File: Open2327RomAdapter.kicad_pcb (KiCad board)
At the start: 2 copper layers, 19.6 x 43.2 mm, 7 parts, among them P1 CONN_01X04, U1 2364, U2 27128

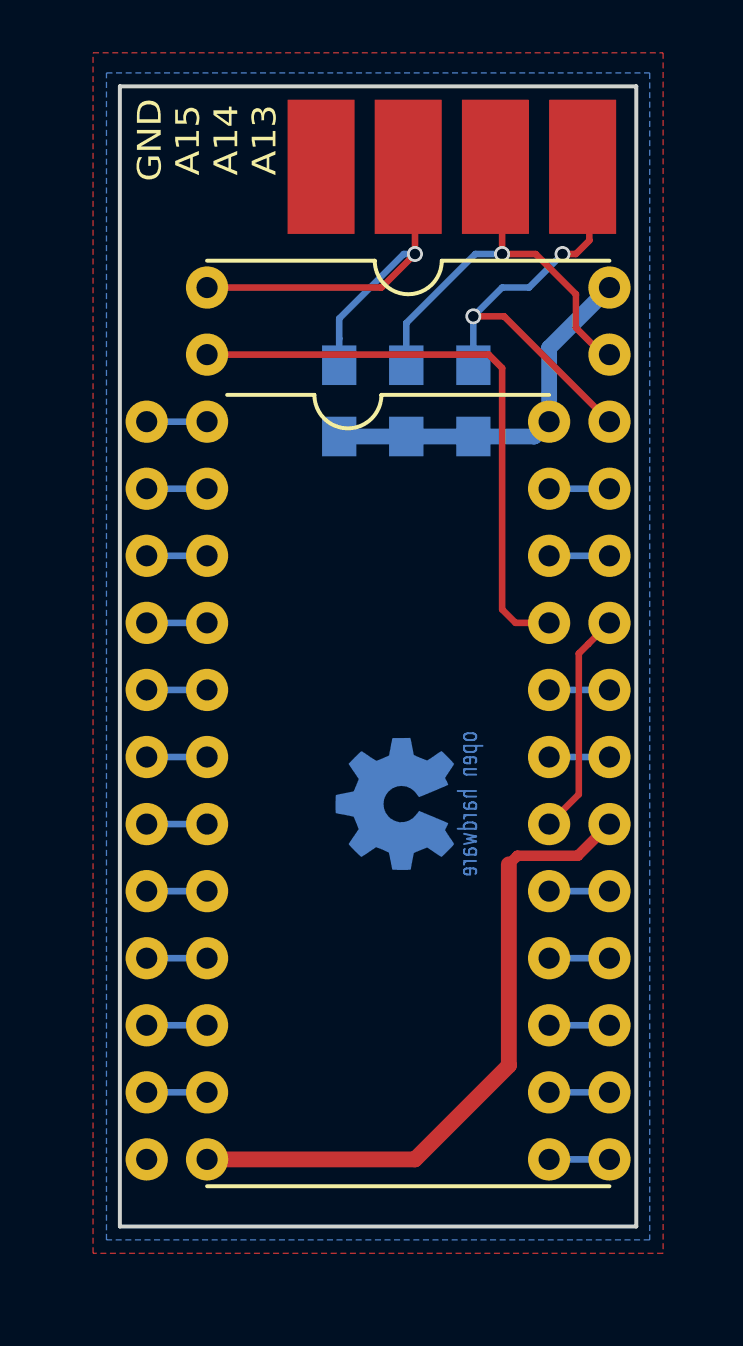
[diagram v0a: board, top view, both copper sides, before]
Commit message: Fix URL, better ground plane, round corners
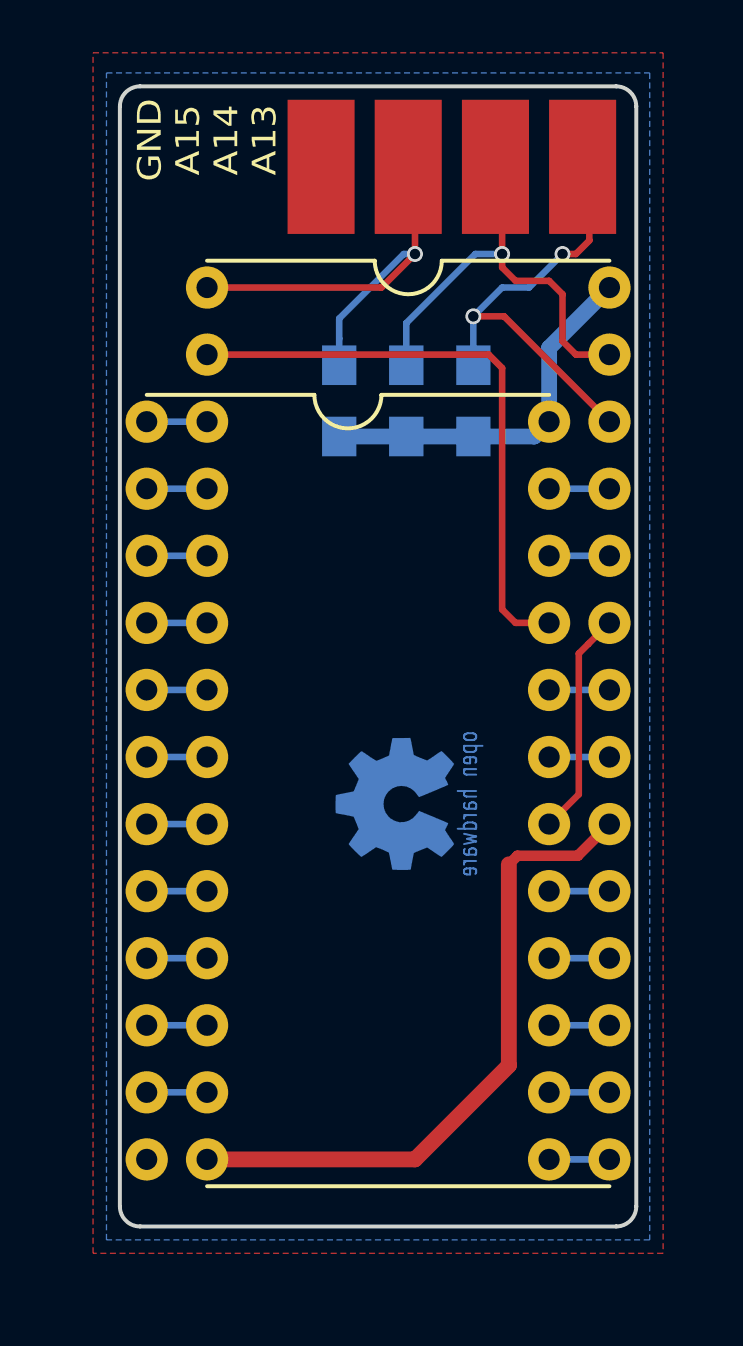
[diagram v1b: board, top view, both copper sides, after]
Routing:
- net Net-(P1-Pad3): track 16.0 -> 16.6 mm
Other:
- outline, holes or cut-outs redrawn
- rule pad_to_mask_clearance: 0.2 -> 0
- board text added: "github.com/SukkoPera/Open2327RomAdapter"
- board text removed: "https://github.com/SukkoPera/Open2327RomAdapter"

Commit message: Final touches for V2
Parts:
- moved G*** 1.48 mm to (154.4, 121.9)
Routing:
- net GND: track 25.0 -> 66.8 mm, vias 0 -> 12
- net Net-(U1-Pad18): track 8.57 -> 12.2 mm
- net Net-(P1-Pad2): track 17.4 -> 16.7 mm
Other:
- board text added: "V2"
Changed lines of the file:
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@@
     (area 145.212999 93.904999 164.921001 137.235001)
     (thickness 1.6)
-    (drawings 13)
-    (tracks 72)
+    (drawings 14)
+    (tracks 95)
     (zones 0)
     (modules 7)
@@
   )
   (page A4)
+  (title_block
+    (title "Open2327RomAdapter: C64 ROM 24 -> EPROM 28 Pin Adapter")
+    (date 2018-01-05)
+    (rev 2)
+    (company SukkoPera)
+    (comment 1 https://ist.uwaterloo.ca/~~schepers/sockets.html)
+    (comment 2 https://ist.uwaterloo.ca/~~schepers/roms.html)
+  )
   (layers
     (0 F.Cu signal)
@@
   )
   (module w_logo:Logo_copper_OSHW_6x6mm (layer B.Cu)
-    (at 155.702 121.158 270)
+    (at 154.432 121.92 270)
     (descr "Open Hardware Logo, 6x6mm")
     (fp_text reference G*** (at 0 0 270) (layer B.SilkS) hide
@@
     )
   )
+  (gr_text V2 (at 163.83 95.504 90) (layer B.SilkS)
+    (effects (font (size 1 1) (thickness 0.15)) (justify mirror))
+  )
   (gr_arc (start 164.084 136.398) (end 164.846 136.398) (angle 90) (layer Edge.Cuts) (width 0.15))
   (gr_arc (start 146.05 136.398) (end 146.05 137.16) (angle 90) (layer Edge.Cuts) (width 0.15))
@@
     (arrow2b (pts (xy 170.18 93.98) (xy 170.766421 95.106504)))
   )
-  (gr_text github.com/SukkoPera/Open2327RomAdapter (at 151.13 115.316 90) (layer B.SilkS)
+  (gr_text github.com/SukkoPera/Open2327RomAdapter (at 150.622 115.316 90) (layer B.SilkS)
     (effects (font (size 1 1) (thickness 0.15)) (justify mirror))
   )
@@
   (gr_line (start 164.846 136.398) (end 164.846 94.742) (layer Edge.Cuts) (width 0.15))
   (gr_line (start 146.05 137.16) (end 164.084 137.16) (layer Edge.Cuts) (width 0.15))
-  (segment (start 160.02 131.064) (end 160.02 123.444) (width 0.6) (layer F.Cu) (net 1))
-  (segment (start 160.343999 123.120001) (end 160.02 123.444) (width 0.4) (layer F.Cu) (net 1))
-  (segment (start 163.83 121.92) (end 162.629999 123.120001) (width 0.4) (layer F.Cu) (net 1))
-  (segment (start 162.629999 123.120001) (end 160.343999 123.120001) (width 0.4) (layer F.Cu) (net 1))
-  (segment (start 156.464 134.62) (end 160.02 131.064) (width 0.6) (layer F.Cu) (net 1))
-  (segment (start 148.59 134.62) (end 156.464 134.62) (width 0.6) (layer F.Cu) (net 1))
+  (segment (start 158.242 134.62) (end 151.892 134.62) (width 0.6) (layer B.Cu) (net 1))
+  (via (at 151.892 134.62) (size 0.8) (drill 0.6) (layers F.Cu B.Cu) (net 1))
+  (segment (start 158.242 129.54) (end 158.242 134.62) (width 0.6) (layer F.Cu) (net 1))
+  (via (at 158.242 134.62) (size 0.8) (drill 0.6) (layers F.Cu B.Cu) (net 1))
+  (segment (start 158.242 124.46) (end 158.242 129.54) (width 0.6) (layer B.Cu) (net 1))
+  (via (at 158.242 129.54) (size 0.8) (drill 0.6) (layers F.Cu B.Cu) (net 1))
+  (segment (start 158.242 119.38) (end 158.242 124.46) (width 0.6) (layer F.Cu) (net 1))
+  (via (at 158.242 124.46) (size 0.8) (drill 0.6) (layers F.Cu B.Cu) (net 1))
+  (segment (start 158.242 114.3) (end 158.242 119.38) (width 0.6) (layer B.Cu) (net 1))
+  (via (at 158.242 119.38) (size 0.8) (drill 0.6) (layers F.Cu B.Cu) (net 1))
+  (segment (start 158.242 109.22) (end 158.242 114.3) (width 0.6) (layer F.Cu) (net 1))
+  (via (at 158.242 114.3) (size 0.8) (drill 0.6) (layers F.Cu B.Cu) (net 1))
+  (segment (start 151.892 109.22) (end 158.242 109.22) (width 0.6) (layer B.Cu) (net 1))
+  (via (at 158.242 109.22) (size 0.8) (drill 0.6) (layers F.Cu B.Cu) (net 1))
+  (segment (start 151.892 114.3) (end 151.892 109.22) (width 0.6) (layer F.Cu) (net 1))
+  (via (at 151.892 109.22) (size 0.8) (drill 0.6) (layers F.Cu B.Cu) (net 1))
+  (segment (start 151.892 119.38) (end 151.892 114.3) (width 0.6) (layer B.Cu) (net 1))
+  (via (at 151.892 114.3) (size 0.8) (drill 0.6) (layers F.Cu B.Cu) (net 1))
+  (segment (start 151.892 124.46) (end 151.892 119.38) (width 0.6) (layer F.Cu) (net 1))
+  (via (at 151.892 119.38) (size 0.8) (drill 0.6) (layers F.Cu B.Cu) (net 1))
+  (segment (start 151.892 129.54) (end 151.892 124.46) (width 0.6) (layer B.Cu) (net 1))
+  (via (at 151.892 124.46) (size 0.8) (drill 0.6) (layers F.Cu B.Cu) (net 1))
+  (segment (start 148.59 134.62) (end 151.892 134.62) (width 0.6) (layer F.Cu) (net 1))
+  (segment (start 151.892 134.62) (end 151.892 129.54) (width 0.6) (layer F.Cu) (net 1))
+  (via (at 151.892 129.54) (size 0.8) (drill 0.6) (layers F.Cu B.Cu) (net 1))
   (segment (start 158.675098 107.241724) (end 160.982276 107.241724) (width 0.6) (layer B.Cu) (net 2))
   (segment (start 160.982276 107.241724) (end 161.544 106.68) (width 0.6) (layer B.Cu) (net 2))
@@
   (segment (start 161.544 127) (end 163.83 127) (width 0.25) (layer B.Cu) (net 17))
   (segment (start 161.544 124.46) (end 163.83 124.46) (width 0.25) (layer B.Cu) (net 18))
-  (segment (start 161.544 121.92) (end 162.669001 120.794999) (width 0.25) (layer F.Cu) (net 19))
-  (segment (start 162.669001 115.460999) (end 163.030001 115.099999) (width 0.25) (layer F.Cu) (net 19))
-  (segment (start 162.669001 120.794999) (end 162.669001 115.460999) (width 0.25) (layer F.Cu) (net 19))
-  (segment (start 163.030001 115.099999) (end 163.83 114.3) (width 0.25) (layer F.Cu) (net 19))
+  (segment (start 161.544 121.92) (end 160.274 121.92) (width 0.25) (layer F.Cu) (net 19))
+  (segment (start 159.766 121.412) (end 159.766 115.968999) (width 0.25) (layer F.Cu) (net 19))
+  (segment (start 160.274 121.92) (end 159.766 121.412) (width 0.25) (layer F.Cu) (net 19))
+  (segment (start 159.766 115.968999) (end 160.274 115.460999) (width 0.25) (layer F.Cu) (net 19))
+  (segment (start 160.274 115.460999) (end 162.669001 115.460999) (width 0.25) (layer F.Cu) (net 19))
+  (segment (start 162.669001 115.460999) (end 163.83 114.3) (width 0.25) (layer F.Cu) (net 19))
   (segment (start 161.544 119.38) (end 163.83 119.38) (width 0.25) (layer B.Cu) (net 20))
   (segment (start 161.544 116.84) (end 163.83 116.84) (width 0.25) (layer B.Cu) (net 21))
@@
   (segment (start 161.544 111.76) (end 163.83 111.76) (width 0.25) (layer B.Cu) (net 23))
   (segment (start 161.544 109.22) (end 163.83 109.22) (width 0.25) (layer B.Cu) (net 24))
-  (segment (start 148.59 101.6) (end 155.194 101.6) (width 0.25) (layer F.Cu) (net 25))
-  (segment (start 155.194 101.6) (end 156.464 100.33) (width 0.25) (layer F.Cu) (net 25))
-  (segment (start 156.464 100.33) (end 156.039736 100.33) (width 0.25) (layer B.Cu) (net 25))
-  (segment (start 156.039736 100.33) (end 153.595098 102.774638) (width 0.25) (layer B.Cu) (net 25))
-  (segment (start 153.595098 102.774638) (end 153.595098 103.541724) (width 0.25) (layer B.Cu) (net 25))
-  (segment (start 153.595098 103.541724) (end 153.595098 104.541724) (width 0.25) (layer B.Cu) (net 25))
-  (via (at 156.464 100.33) (size 0.6) (drill 0.4) (layers F.Cu B.Cu) (net 25))
-  (segment (start 156.464 97.028) (end 156.464 100.33) (width 0.25) (layer F.Cu) (net 25))
-  (segment (start 159.766 100.33) (end 159.766 100.838) (width 0.25) (layer F.Cu) (net 26))
-  (segment (start 159.766 100.838) (end 160.274 101.346) (width 0.25) (layer F.Cu) (net 26))
-  (segment (start 160.274 101.346) (end 161.544 101.346) (width 0.25) (layer F.Cu) (net 26))
+  (segment (start 153.595098 104.541724) (end 153.595098 102.944902) (width 0.25) (layer B.Cu) (net 25))
+  (segment (start 153.595098 102.944902) (end 153.924 102.616) (width 0.25) (layer B.Cu) (net 25))
+  (segment (start 153.924 102.616) (end 156.21 100.33) (width 0.25) (layer B.Cu) (net 25))
+  (via (at 156.21 100.33) (size 0.6) (drill 0.4) (layers F.Cu B.Cu) (net 25))
+  (segment (start 148.59 101.6) (end 154.94 101.6) (width 0.25) (layer F.Cu) (net 25))
+  (segment (start 156.21 100.33) (end 154.94 101.6) (width 0.25) (layer F.Cu) (net 25))
+  (segment (start 156.21 97.028) (end 156.21 100.33) (width 0.25) (layer F.Cu) (net 25))
+  (segment (start 160.528 101.346) (end 161.544 101.346) (width 0.25) (layer F.Cu) (net 26))
+  (segment (start 159.512 100.33) (end 159.512 100.754264) (width 0.25) (layer F.Cu) (net 26))
+  (segment (start 159.512 100.754264) (end 160.103736 101.346) (width 0.25) (layer F.Cu) (net 26))
+  (segment (start 160.103736 101.346) (end 160.528 101.346) (width 0.25) (layer F.Cu) (net 26))
+  (segment (start 159.512 100.33) (end 158.75 100.33) (width 0.25) (layer B.Cu) (net 26))
+  (segment (start 159.512 97.028) (end 159.512 100.33) (width 0.25) (layer F.Cu) (net 26))
+  (via (at 159.512 100.33) (size 0.6) (drill 0.4) (layers F.Cu B.Cu) (net 26))
   (segment (start 162.56 104.14) (end 163.83 104.14) (width 0.25) (layer F.Cu) (net 26))
   (segment (start 161.544 101.346) (end 162.052 101.854) (width 0.25) (layer F.Cu) (net 26))
   (segment (start 162.052 101.854) (end 162.052 103.632) (width 0.25) (layer F.Cu) (net 26))
   (segment (start 162.052 103.632) (end 162.56 104.14) (width 0.25) (layer F.Cu) (net 26))
-  (segment (start 159.766 97.028) (end 159.766 100.33) (width 0.25) (layer F.Cu) (net 26))
-  (via (at 159.766 100.33) (size 0.6) (drill 0.4) (layers F.Cu B.Cu) (net 26))
   (segment (start 158.75 100.33) (end 156.135098 102.944902) (width 0.25) (layer B.Cu) (net 26))
-  (segment (start 159.766 100.33) (end 158.75 100.33) (width 0.25) (layer B.Cu) (net 26))
   (segment (start 156.135098 102.944902) (end 156.135098 104.541724) (width 0.25) (layer B.Cu) (net 26))
+  (segment (start 162.814 99.818) (end 162.81 99.822) (width 0.25) (layer F.Cu) (net 27))
+  (segment (start 162.81 100.076) (end 162.556 100.33) (width 0.25) (layer F.Cu) (net 27))
+  (segment (start 162.814 97.028) (end 162.814 99.818) (width 0.25) (layer F.Cu) (net 27))
+  (segment (start 162.81 99.822) (end 162.81 100.076) (width 0.25) (layer F.Cu) (net 27))
   (segment (start 162.556 100.33) (end 162.052 100.33) (width 0.25) (layer F.Cu) (net 27))
-  (segment (start 163.068 97.028) (end 163.068 99.818) (width 0.25) (layer F.Cu) (net 27))
-  (segment (start 163.068 99.818) (end 162.556 100.33) (width 0.25) (layer F.Cu) (net 27))
   (via (at 162.052 100.33) (size 0.6) (drill 0.4) (layers F.Cu B.Cu) (net 27))
   (segment (start 162.052 100.33) (end 160.782 101.6) (width 0.25) (layer B.Cu) (net 27))

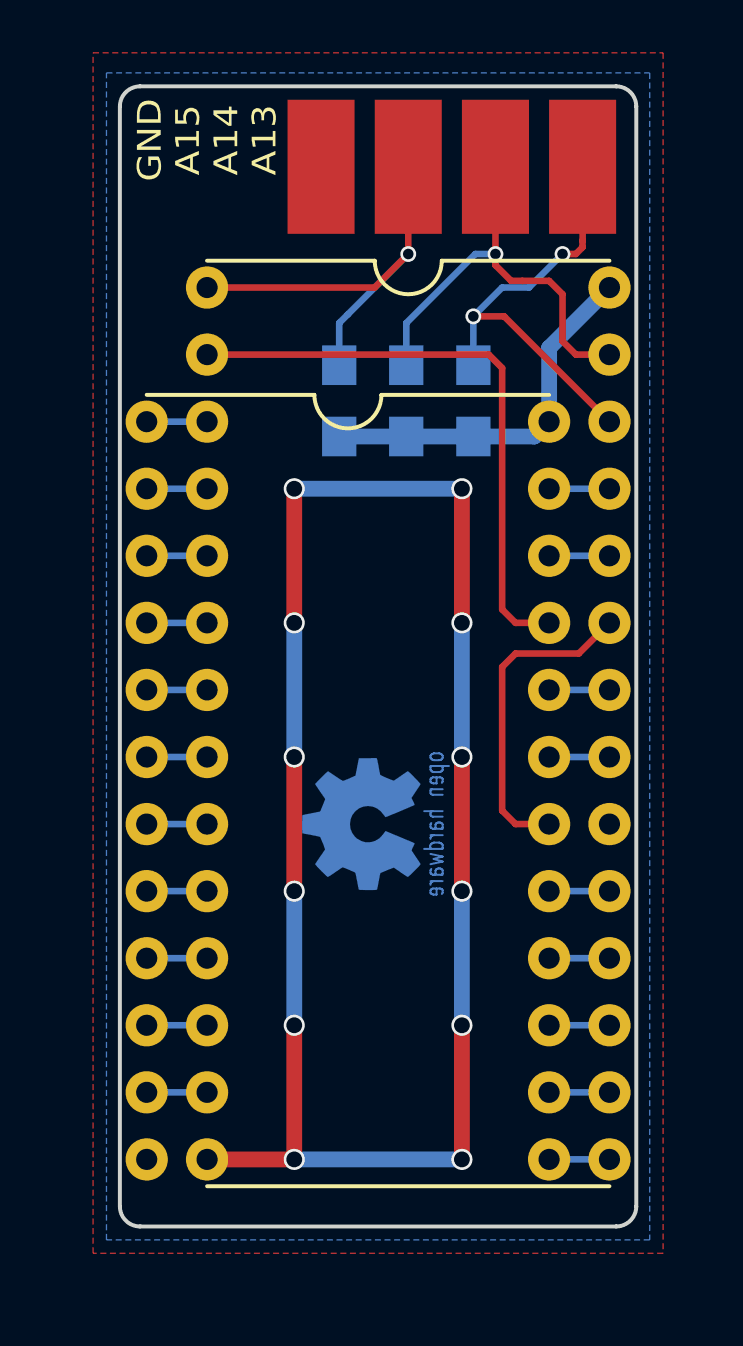
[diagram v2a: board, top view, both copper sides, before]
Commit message: Move solderable pads to 0.1" pitch and drill a hole through them Also port to Kicad 5 and use builtin components/footprints
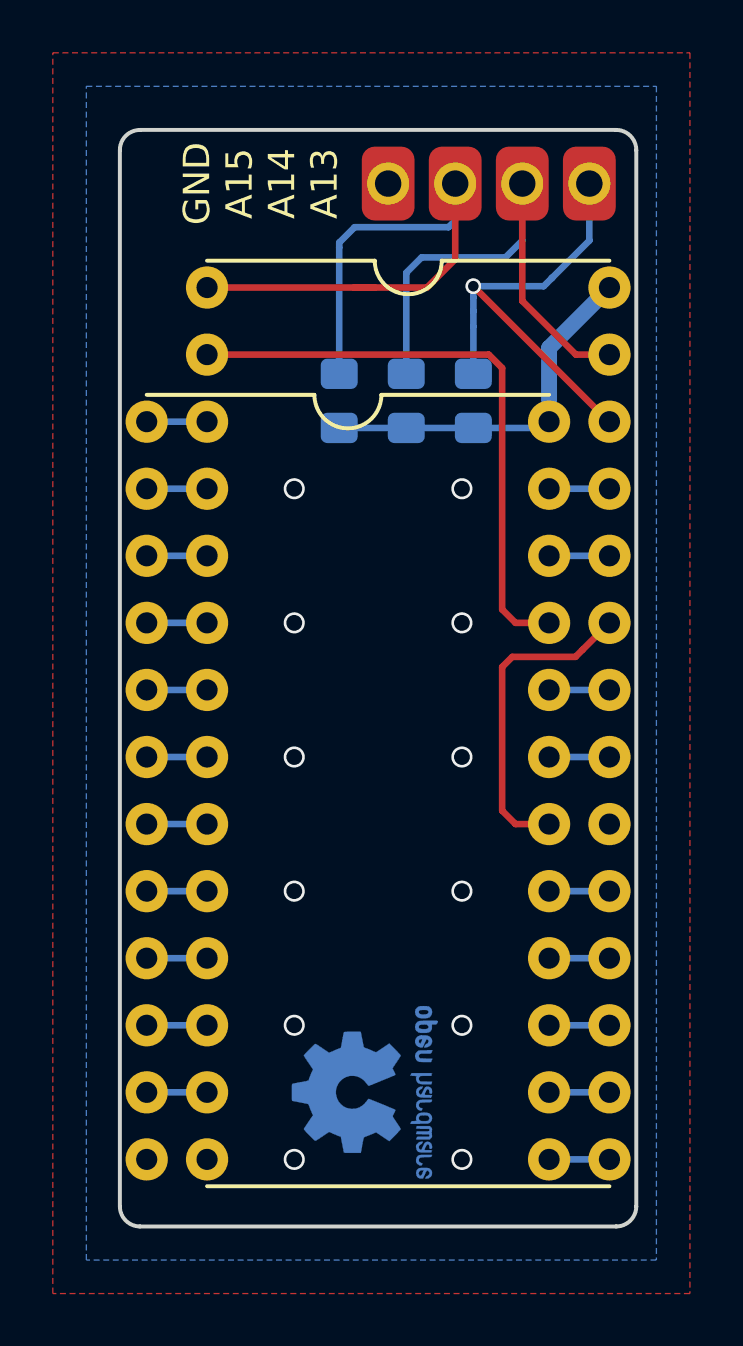
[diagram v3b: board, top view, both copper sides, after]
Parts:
- removed G***: LOGO, w_logo:Logo_copper_OSHW_6x6mm
- added P99: OSHW_LOGO, Symbol:OSHW-Logo2_7.3x6mm_Copper, B.Cu at (154.6, 132.1)
- P1: value CONN_01X04 -> Conn_01x04; footprint Open2327RomAdapter:LoosePads-4 -> Open2327RomAdapter:Solderable_PinHeader_1x04
- R1, R2, R3: value 10K -> 10k; footprint Resistors_SMD:R_0805_HandSoldering -> Resistor_SMD:R_0805_2012Metric_Pad1.15x1.40mm_HandSolder
- moved P1 2.62 mm to (155.4, 97.7), turned to 90 degrees
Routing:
- net GND: track 66.8 -> 0.00 mm
- net Net-(P1-Pad2): track 16.7 -> 24.6 mm, vias 1 -> 0
- net Net-(P1-Pad3): track 16.5 -> 19.5 mm, vias 1 -> 0
- net Net-(P1-Pad4): track 16.9 -> 17.9 mm, vias 2 -> 1
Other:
- board size 19.6 x 43.2 mm -> 19.6 x 41.5 mm
- board text added: "Licensed under CERN OHL v.1.2"
- board text added: "V3"
- board text removed: "V2"
